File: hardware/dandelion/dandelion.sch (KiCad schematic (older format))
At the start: 104 parts, among them J1 PCB antenna, J2 USB-MICRO-B, P1 DIGITAL, P10 GIO6, P11 DCLK, P12 DIO, P13 PCB JUMPER, P14 E8A, P15 R8C PROGRAM, P16 R8C EXPAND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

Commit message: Dandelion: LPC1756 recommendation note
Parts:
- U4: Field2 LPC1752FBD80,551 -> LPC1756FBD80,551
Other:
- note added: "U4: LPC1756 or better is recommended\nAny of the following should work:\nLPC1752, LPC1754, LPC1756, LPC1758, LPC1759"
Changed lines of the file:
@@
-EESchema Schematic File Version 2  date Mon 29 Aug 2011 02:44:30 PM MDT
+EESchema Schematic File Version 2  date Mon 29 Aug 2011 02:51:23 PM MDT
 LIBS:ubertooth-symbols
 LIBS:power
@@
 Comment4 ""
 $EndDescr
+Text Notes 6250 3000 0    60   ~ 0
+U4: LPC1756 or better is recommended\nAny of the following should work:\nLPC1752, LPC1754, LPC1756, LPC1758, LPC1759
 $Comp
 L CONN_1 P18
@@
 F 2 "LQFP80" H 9550 5650 60  0001 C CNN
 F 4 "NXP" H 9550 5650 60  0001 C CNN "Field1"
-F 5 "LPC1752FBD80,551" H 9550 5650 60  0001 C CNN "Field2"
+F 5 "LPC1756FBD80,551" H 9550 5650 60  0001 C CNN "Field2"
 F 6 "Microcontrollers (MCU) ARM Cortex M3 Micro Controller" H 9550 5650 60  0001 C CNN "Field3"
 F 7 "DIY" H 9550 5650 60  0001 C CNN "Field4"

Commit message: Dandelion: back annotation of module info into schematic
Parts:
- BT1: footprint (none) -> GSG-BK-912
- C1, C2: footprint (none) -> GSG-1206
- C12, C17, C18, C19, C3, C6, C7, C8, L1, R22: footprint (none) -> 0402
- C15: footprint (none) -> GSG-UUR1C101MCL1GS
- C20, C21: footprint (none) -> 0603
- D1, D10, D11, D12, D13, D2, D3, D4, D5, D6, D7, D8, D9: footprint (none) -> GSG-1206D
- D16, D18: footprint (none) -> GSG-SOD-523F
- J1: footprint (none) -> GSG-2.4GHz-FOLDED-DIPOLE
- J2: footprint (none) -> GSG-USB-MICROB-FCI-10103594
- L4: footprint (none) -> 0402gap
- P1, P16: footprint (none) -> PIN_ARRAY_5x2
- P13: footprint (none) -> 0603bridged
- P14: footprint (none) -> PIN_ARRAY-4X1
- P15, P2: footprint 100MIL-HEADER-1X6-EDGE -> PIN_ARRAY-6X1
- Q2: footprint (none) -> SOT23GDS
- SW1: footprint (none) -> GSG-SPST-FSM4JSMATR
- U1: footprint (none) -> GSG-SC70-5
- U2: footprint (none) -> SOT23-5
- U3: footprint (none) -> QFN48
- U5: footprint (none) -> GSG-P-LQFP32-7x7-0.80
- X1: footprint (none) -> GSG-HC-49S

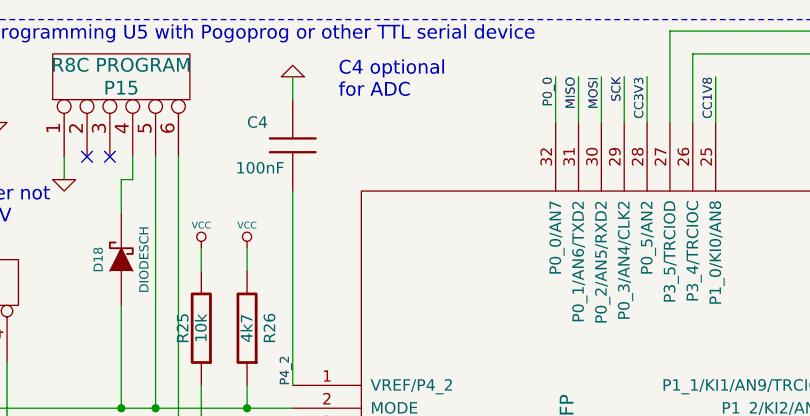
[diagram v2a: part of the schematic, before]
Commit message: Dandelion: added VREF to VCC PCB jumper
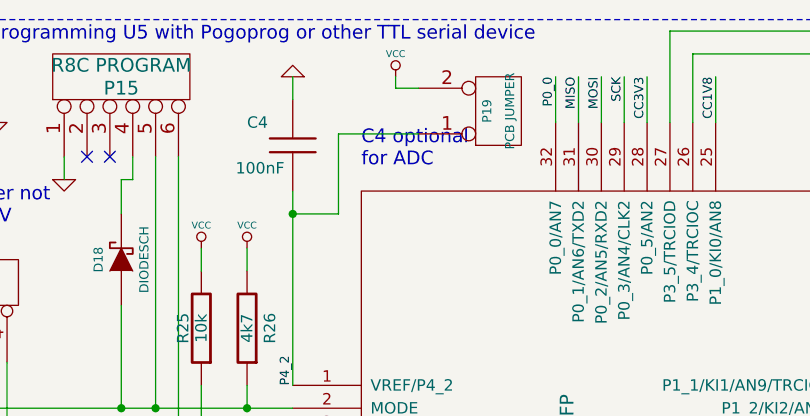
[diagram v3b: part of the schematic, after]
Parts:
- added P19: PCB JUMPER, 0603bridged, symbol CONN_2
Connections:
- net P4_2: now also P19.1 (P1)
- net VCC: now also P19.2 (PM)
